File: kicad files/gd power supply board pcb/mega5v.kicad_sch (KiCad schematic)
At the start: 14 parts

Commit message: before erc
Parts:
- added H10, H11, H12, H9: MountingHole, MountingHole:MountingHole_2.2mm_M2, symbol Mechanical:MountingHole
- gave numbers to parts that had none: 14
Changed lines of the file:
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@@
   (symbol (lib_id "Device:R_Small") (at 171.45 105.41 180) (unit 1)
     (in_bom yes) (on_board yes)
-    (property "Reference" "R?" (id 0) (at 172.9486 104.2416 0)
+    (property "Reference" "R23" (id 0) (at 172.9486 104.2416 0)
       (effects (font (size 1.27 1.27)) (justify right))
     )
@@
     (pin "2")
   )
+  (symbol (lib_id "Mechanical:MountingHole") (at 200.66 53.34 0) (unit 1)
+    (in_bom yes) (on_board yes) (fields_autoplaced)
+    (property "Reference" "H9" (id 0) (at 203.2 52.0699 0)
+      (effects (font (size 1.27 1.27)) (justify left))
+    )
+    (property "Value" "MountingHole" (id 1) (at 203.2 54.6099 0)
+      (effects (font (size 1.27 1.27)) (justify left))
+    )
+    (property "Footprint" "MountingHole:MountingHole_2.2mm_M2" (id 2) (at 200.66 53.34 0)
+      (effects (font (size 1.27 1.27)) hide)
+    )
+    (property "Datasheet" "~" (id 3) (at 200.66 53.34 0)
+      (effects (font (size 1.27 1.27)) hide)
+    )
+  )
   (symbol (lib_id "My Library:TestPoint_Harwin") (at 171.45 93.98 0) (unit 1)
     (in_bom yes) (on_board yes)
-    (property "Reference" "TP?" (id 0) (at 170.18 88.9 0)
+    (property "Reference" "TP25" (id 0) (at 170.18 88.9 0)
       (effects (font (size 1.27 1.27)) (justify left))
     )
@@
   (symbol (lib_id "power:GND") (at 171.45 109.728 0) (unit 1)
     (in_bom yes) (on_board yes)
-    (property "Reference" "#PWR?" (id 0) (at 171.45 116.078 0)
+    (property "Reference" "#PWR05" (id 0) (at 171.45 116.078 0)
       (effects (font (size 1.27 1.27)) hide)
     )
@@
   (symbol (lib_id "My Library:TestPoint_Harwin") (at 125.73 99.06 180) (unit 1)
     (in_bom yes) (on_board yes)
-    (property "Reference" "TP?" (id 0) (at 124.46 105.41 0)
+    (property "Reference" "TP22" (id 0) (at 124.46 105.41 0)
       (effects (font (size 1.27 1.27)) (justify right))
     )
@@
   (symbol (lib_id "power:GND") (at 195.58 101.854 0) (unit 1)
     (in_bom yes) (on_board yes)
-    (property "Reference" "#PWR?" (id 0) (at 195.58 108.204 0)
+    (property "Reference" "#PWR07" (id 0) (at 195.58 108.204 0)
       (effects (font (size 1.27 1.27)) hide)
     )
@@
   (symbol (lib_id "Device:R_Small") (at 171.45 97.282 180) (unit 1)
     (in_bom yes) (on_board yes)
-    (property "Reference" "R?" (id 0) (at 172.9486 96.1136 0)
+    (property "Reference" "R22" (id 0) (at 172.9486 96.1136 0)
       (effects (font (size 1.27 1.27)) (justify right))
     )
@@
   (symbol (lib_id "Device:L_Small") (at 165.1 93.98 90) (unit 1)
     (in_bom yes) (on_board yes)
-    (property "Reference" "L?" (id 0) (at 165.1 89.281 90))
+    (property "Reference" "L3" (id 0) (at 165.1 89.281 90))
     (property "Value" "1.5u" (id 1) (at 165.1 91.5924 90))
     (property "Footprint" "Inductor_SMD:L_Bourns_SRP5030T" (id 2) (at 165.1 93.98 0)
@@
   (symbol (lib_id "power:GND") (at 100.33 102.87 0) (unit 1)
     (in_bom yes) (on_board yes)
-    (property "Reference" "#PWR?" (id 0) (at 100.33 109.22 0)
+    (property "Reference" "#PWR02" (id 0) (at 100.33 109.22 0)
       (effects (font (size 1.27 1.27)) hide)
     )
@@
   (symbol (lib_id "Device:C_Small") (at 154.94 85.344 0) (unit 1)
     (in_bom yes) (on_board yes)
-    (property "Reference" "C?" (id 0) (at 157.2768 84.1756 0)
+    (property "Reference" "C14" (id 0) (at 157.2768 84.1756 0)
       (effects (font (size 1.27 1.27)) (justify left))
     )
@@
   (symbol (lib_id "My Library:TestPoint_Harwin") (at 158.75 99.06 180) (unit 1)
     (in_bom yes) (on_board yes) (fields_autoplaced)
-    (property "Reference" "TP?" (id 0) (at 161.29 102.3619 0)
+    (property "Reference" "TP24" (id 0) (at 161.29 102.3619 0)
       (effects (font (size 1.27 1.27)) (justify right))
     )
@@
   (symbol (lib_id "Device:C_Small") (at 109.22 99.06 0) (unit 1)
     (in_bom yes) (on_board yes)
-    (property "Reference" "C?" (id 0) (at 111.5568 97.8916 0)
+    (property "Reference" "C13" (id 0) (at 111.5568 97.8916 0)
       (effects (font (size 1.27 1.27)) (justify left))
     )
@@
   (symbol (lib_id "Device:C_Small") (at 195.58 97.536 0) (unit 1)
     (in_bom yes) (on_board yes)
-    (property "Reference" "C?" (id 0) (at 197.9168 96.3676 0)
+    (property "Reference" "C16" (id 0) (at 197.9168 96.3676 0)
       (effects (font (size 1.27 1.27)) (justify left))
     )
@@
   (symbol (lib_id "My Library:TestPoint_Harwin") (at 109.22 93.98 0) (unit 1)
     (in_bom yes) (on_board yes)
-    (property "Reference" "TP?" (id 0) (at 107.95 88.9 0)
+    (property "Reference" "TP21" (id 0) (at 107.95 88.9 0)
       (effects (font (size 1.27 1.27)) (justify left))
     )
@@
   (symbol (lib_id "TO3-Switching-Supply-rescue:TPS563200-Regulator_Switching") (at 137.16 96.52 0) (unit 1)
     (in_bom yes) (on_board yes)
-    (property "Reference" "U?" (id 0) (at 137.16 87.1982 0))
+    (property "Reference" "U3" (id 0) (at 137.16 87.1982 0))
     (property "Value" "TPS563240DDCR" (id 1) (at 137.16 89.5096 0))
     (property "Footprint" "Package_TO_SOT_SMD:SOT-23-6" (id 2) (at 138.43 102.87 0)
@@
   (symbol (lib_id "Device:C_Small") (at 185.42 97.79 0) (unit 1)
     (in_bom yes) (on_board yes)
-    (property "Reference" "C?" (id 0) (at 187.7568 96.6216 0)
+    (property "Reference" "C15" (id 0) (at 187.7568 96.6216 0)
       (effects (font (size 1.27 1.27)) (justify left))
     )
@@
   (symbol (lib_id "power:GND") (at 109.22 102.87 0) (unit 1)
     (in_bom yes) (on_board yes)
-    (property "Reference" "#PWR?" (id 0) (at 109.22 109.22 0)
+    (property "Reference" "#PWR03" (id 0) (at 109.22 109.22 0)
       (effects (font (size 1.27 1.27)) hide)
     )
@@
   (symbol (lib_id "power:GND") (at 137.16 106.68 0) (unit 1)
     (in_bom yes) (on_board yes)
-    (property "Reference" "#PWR?" (id 0) (at 137.16 113.03 0)
+    (property "Reference" "#PWR04" (id 0) (at 137.16 113.03 0)
       (effects (font (size 1.27 1.27)) hide)
     )
@@
   (symbol (lib_id "power:GND") (at 185.42 102.108 0) (unit 1)
     (in_bom yes) (on_board yes)
-    (property "Reference" "#PWR?" (id 0) (at 185.42 108.458 0)
+    (property "Reference" "#PWR06" (id 0) (at 185.42 108.458 0)
       (effects (font (size 1.27 1.27)) hide)
     )
@@
     (pin "1")
   )
+  (symbol (lib_id "Mechanical:MountingHole") (at 209.55 53.34 0) (unit 1)
+    (in_bom yes) (on_board yes) (fields_autoplaced)
+    (property "Reference" "H11" (id 0) (at 212.09 52.0699 0)
+      (effects (font (size 1.27 1.27)) (justify left))
+    )
+    (property "Value" "MountingHole" (id 1) (at 212.09 54.6099 0)
+      (effects (font (size 1.27 1.27)) (justify left))
+    )
+    (property "Footprint" "MountingHole:MountingHole_2.2mm_M2" (id 2) (at 209.55 53.34 0)
+      (effects (font (size 1.27 1.27)) hide)
+    )
+    (property "Datasheet" "~" (id 3) (at 209.55 53.34 0)
+      (effects (font (size 1.27 1.27)) hide)
+    )
+  )
   (symbol (lib_id "My Library:TestPoint_Harwin") (at 158.75 93.98 0) (unit 1)
     (in_bom yes) (on_board yes)
-    (property "Reference" "TP?" (id 0) (at 157.48 88.9 0)
+    (property "Reference" "TP23" (id 0) (at 157.48 88.9 0)
       (effects (font (size 1.27 1.27)) (justify left))
     )
@@
     (pin "1")
   )
+  (symbol (lib_id "Mechanical:MountingHole") (at 209.55 59.69 0) (unit 1)
+    (in_bom yes) (on_board yes) (fields_autoplaced)
+    (property "Reference" "H12" (id 0) (at 212.09 58.4199 0)
+      (effects (font (size 1.27 1.27)) (justify left))
+    )
+    (property "Value" "MountingHole" (id 1) (at 212.09 60.9599 0)
+      (effects (font (size 1.27 1.27)) (justify left))
+    )
+    (property "Footprint" "MountingHole:MountingHole_2.2mm_M2" (id 2) (at 209.55 59.69 0)
+      (effects (font (size 1.27 1.27)) hide)
+    )
+    (property "Datasheet" "~" (id 3) (at 209.55 59.69 0)
+      (effects (font (size 1.27 1.27)) hide)
+    )
+  )
   (symbol (lib_id "Device:C_Small") (at 100.33 97.79 0) (unit 1)
     (in_bom yes) (on_board yes)
-    (property "Reference" "C?" (id 0) (at 102.6668 96.6216 0)
+    (property "Reference" "C12" (id 0) (at 102.6668 96.6216 0)
       (effects (font (size 1.27 1.27)) (justify left))
     )
@@
     (pin "2")
   )
+  (symbol (lib_id "Mechanical:MountingHole") (at 200.66 59.69 0) (unit 1)
+    (in_bom yes) (on_board yes) (fields_autoplaced)
+    (property "Reference" "H10" (id 0) (at 203.2 58.4199 0)
+      (effects (font (size 1.27 1.27)) (justify left))
+    )
+    (property "Value" "MountingHole" (id 1) (at 203.2 60.9599 0)
+      (effects (font (size 1.27 1.27)) (justify left))
+    )
+    (property "Footprint" "MountingHole:MountingHole_2.2mm_M2" (id 2) (at 200.66 59.69 0)
+      (effects (font (size 1.27 1.27)) hide)
+    )
+    (property "Datasheet" "~" (id 3) (at 200.66 59.69 0)
+      (effects (font (size 1.27 1.27)) hide)
+    )
+  )
 )

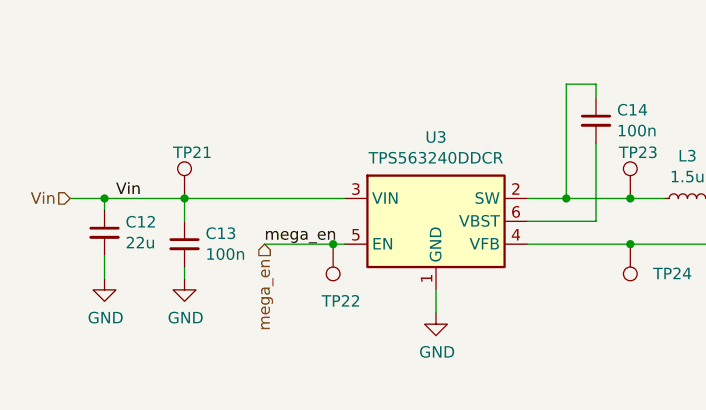
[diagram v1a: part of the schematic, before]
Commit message: initial floor planning done
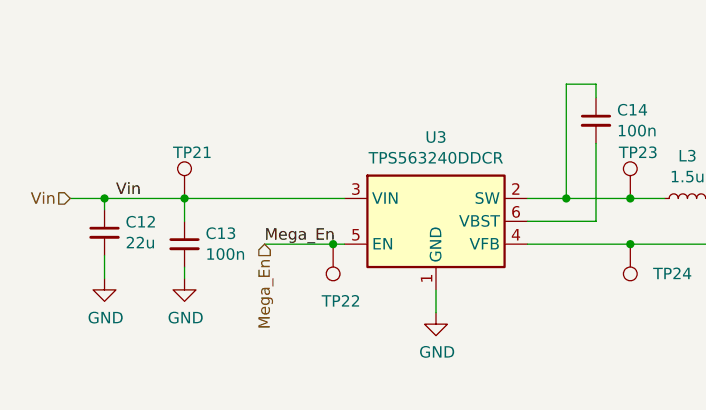
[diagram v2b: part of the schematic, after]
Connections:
- net mega_en renamed Mega_En
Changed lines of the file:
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@@
     (effects (font (size 1.27 1.27)) (justify left bottom))
   )
-  (label "mega_en" (at 118.11 99.06 0)
+  (label "Mega_En" (at 118.11 99.06 0)
     (effects (font (size 1.27 1.27)) (justify left bottom))
   )
@@
     (effects (font (size 1.27 1.27)) (justify right))
   )
-  (hierarchical_label "mega_en" (shape input) (at 118.11 99.06 270)
+  (hierarchical_label "Mega_En" (shape input) (at 118.11 99.06 270)
     (effects (font (size 1.27 1.27)) (justify right))
   )

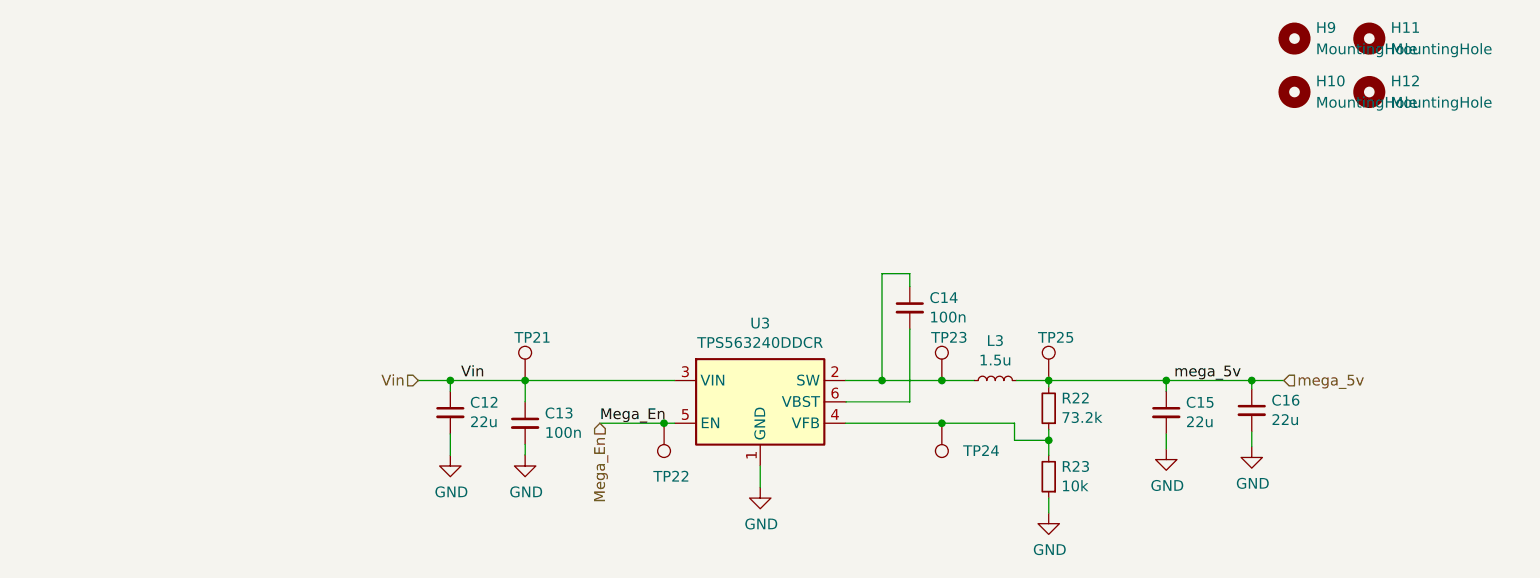
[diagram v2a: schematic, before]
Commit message: minor fixes and compacting the floorplan. stacked 5V supplies for maximum minimage.
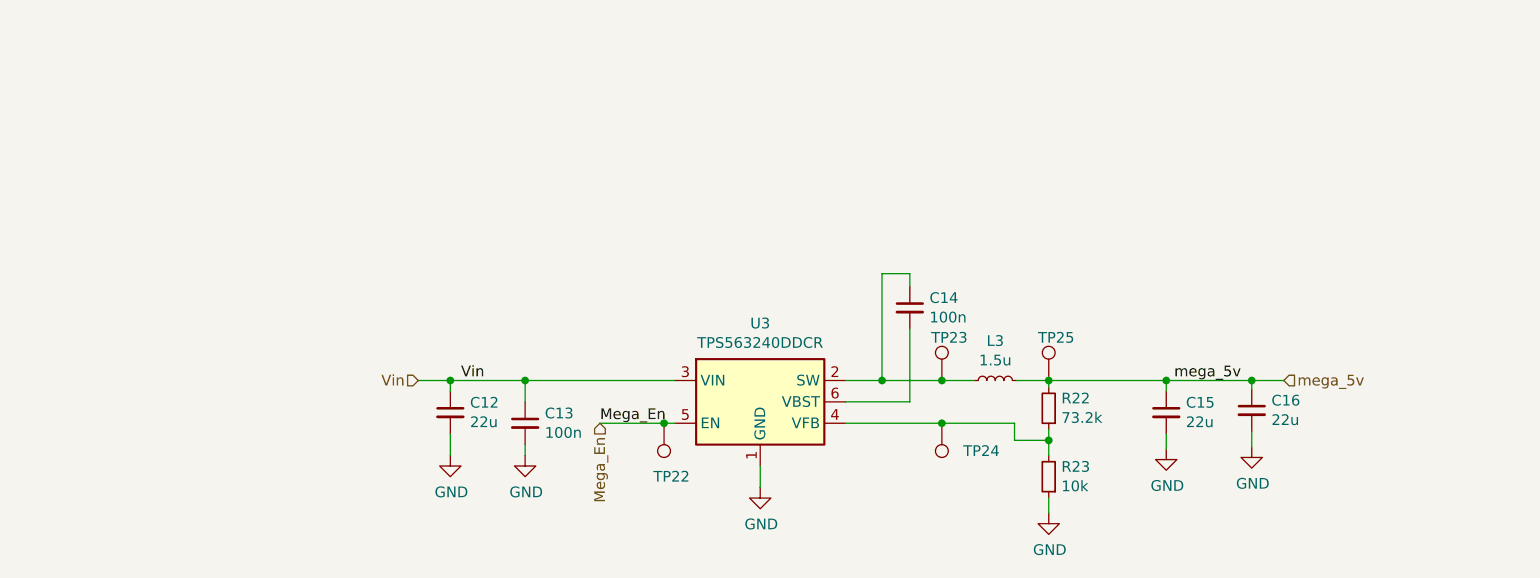
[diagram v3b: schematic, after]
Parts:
- removed H10, H11, H12, H9: MountingHole, MountingHole:MountingHole_2.2mm_M2, symbol Mechanical:MountingHole
- removed TP21: TestPoint_Harwin, My Libraries:Harwin-S1751-46-Test-Point, symbol My Library:TestPoint_Harwin
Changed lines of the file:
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@@
     (pin "2")
-  )
-  (symbol (lib_id "Mechanical:MountingHole") (at 200.66 53.34 0) (unit 1)
-    (in_bom yes) (on_board yes) (fields_autoplaced)
-    (property "Reference" "H9" (id 0) (at 203.2 52.0699 0)
-      (effects (font (size 1.27 1.27)) (justify left))
-    )
-    (property "Value" "MountingHole" (id 1) (at 203.2 54.6099 0)
-      (effects (font (size 1.27 1.27)) (justify left))
-    )
-    (property "Footprint" "MountingHole:MountingHole_2.2mm_M2" (id 2) (at 200.66 53.34 0)
-      (effects (font (size 1.27 1.27)) hide)
-    )
-    (property "Datasheet" "~" (id 3) (at 200.66 53.34 0)
-      (effects (font (size 1.27 1.27)) hide)
-    )
   )
   (symbol (lib_id "My Library:TestPoint_Harwin") (at 171.45 93.98 0) (unit 1)
@@
     (pin "1")
     (pin "2")
-  )
-  (symbol (lib_id "My Library:TestPoint_Harwin") (at 109.22 93.98 0) (unit 1)
-    (in_bom yes) (on_board yes)
-    (property "Reference" "TP21" (id 0) (at 107.95 88.9 0)
-      (effects (font (size 1.27 1.27)) (justify left))
-    )
-    (property "Value" "TestPoint_Harwin" (id 1) (at 109.22 88.9 0)
-      (effects (font (size 1.27 1.27)) hide)
-    )
-    (property "Footprint" "My Libraries:Harwin-S1751-46-Test-Point" (id 2) (at 114.3 93.98 0)
-      (effects (font (size 1.27 1.27)) hide)
-    )
-    (property "Datasheet" "~" (id 3) (at 114.3 93.98 0)
-      (effects (font (size 1.27 1.27)) hide)
-    )
-    (pin "1")
   )
   (symbol (lib_id "TO3-Switching-Supply-rescue:TPS563200-Regulator_Switching") (at 137.16 96.52 0) (unit 1)
@@
     (pin "1")
   )
-  (symbol (lib_id "Mechanical:MountingHole") (at 209.55 53.34 0) (unit 1)
-    (in_bom yes) (on_board yes) (fields_autoplaced)
-    (property "Reference" "H11" (id 0) (at 212.09 52.0699 0)
-      (effects (font (size 1.27 1.27)) (justify left))
-    )
-    (property "Value" "MountingHole" (id 1) (at 212.09 54.6099 0)
-      (effects (font (size 1.27 1.27)) (justify left))
-    )
-    (property "Footprint" "MountingHole:MountingHole_2.2mm_M2" (id 2) (at 209.55 53.34 0)
-      (effects (font (size 1.27 1.27)) hide)
-    )
-    (property "Datasheet" "~" (id 3) (at 209.55 53.34 0)
-      (effects (font (size 1.27 1.27)) hide)
-    )
-  )
   (symbol (lib_id "My Library:TestPoint_Harwin") (at 158.75 93.98 0) (unit 1)
     (in_bom yes) (on_board yes)
@@
     (pin "1")
   )
-  (symbol (lib_id "Mechanical:MountingHole") (at 209.55 59.69 0) (unit 1)
-    (in_bom yes) (on_board yes) (fields_autoplaced)
-    (property "Reference" "H12" (id 0) (at 212.09 58.4199 0)
-      (effects (font (size 1.27 1.27)) (justify left))
-    )
-    (property "Value" "MountingHole" (id 1) (at 212.09 60.9599 0)
-      (effects (font (size 1.27 1.27)) (justify left))
-    )
-    (property "Footprint" "MountingHole:MountingHole_2.2mm_M2" (id 2) (at 209.55 59.69 0)
-      (effects (font (size 1.27 1.27)) hide)
-    )
-    (property "Datasheet" "~" (id 3) (at 209.55 59.69 0)
-      (effects (font (size 1.27 1.27)) hide)
-    )
-  )
   (symbol (lib_id "Device:C_Small") (at 100.33 97.79 0) (unit 1)
     (in_bom yes) (on_board yes)
@@
     (pin "2")
   )
-  (symbol (lib_id "Mechanical:MountingHole") (at 200.66 59.69 0) (unit 1)
-    (in_bom yes) (on_board yes) (fields_autoplaced)
-    (property "Reference" "H10" (id 0) (at 203.2 58.4199 0)
-      (effects (font (size 1.27 1.27)) (justify left))
-    )
-    (property "Value" "MountingHole" (id 1) (at 203.2 60.9599 0)
-      (effects (font (size 1.27 1.27)) (justify left))
-    )
-    (property "Footprint" "MountingHole:MountingHole_2.2mm_M2" (id 2) (at 200.66 59.69 0)
-      (effects (font (size 1.27 1.27)) hide)
-    )
-    (property "Datasheet" "~" (id 3) (at 200.66 59.69 0)
-      (effects (font (size 1.27 1.27)) hide)
-    )
-  )
 )

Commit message: pre-routing try 1
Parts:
- added JP4: mega_5v_jmp, Jumper:SolderJumper-2_P1.3mm_Open_TrianglePad1.0x1.5mm, symbol Jumper:Jumper_2_Open
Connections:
- net Vin: now also JP4.1 (A); no longer C12.1, C13.1, U3.3 (VIN)
- new net: C12.1, C13.1, JP4.2 (B), U3.3 (VIN)
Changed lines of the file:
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@@
+    (stroke (width 0) (type default) (color 0 0 0 0))
+  )
+  (wire (pts (xy 81.28 93.98) (xy 83.82 93.98))
     (stroke (width 0) (type default) (color 0 0 0 0))
   )
@@
     (stroke (width 0) (type default) (color 0 0 0 0))
   )
-  (wire (pts (xy 96.52 93.98) (xy 100.33 93.98))
+  (wire (pts (xy 93.98 93.98) (xy 100.33 93.98))
     (stroke (width 0) (type default) (color 0 0 0 0))
   )
@@
     (effects (font (size 1.27 1.27)) (justify right bottom))
   )
-  (label "Vin" (at 101.6 93.98 0)
-    (effects (font (size 1.27 1.27)) (justify left bottom))
-  )
   (label "Mega_En" (at 118.11 99.06 0)
     (effects (font (size 1.27 1.27)) (justify left bottom))
   )
-  (hierarchical_label "Vin" (shape input) (at 96.52 93.98 180)
-    (effects (font (size 1.27 1.27)) (justify right))
-  )
   (hierarchical_label "Mega_En" (shape input) (at 118.11 99.06 270)
     (effects (font (size 1.27 1.27)) (justify right))
@@
   (hierarchical_label "mega_5v" (shape input) (at 199.39 93.98 0)
     (effects (font (size 1.27 1.27)) (justify left))
+  )
+  (hierarchical_label "Vin" (shape input) (at 81.28 93.98 180)
+    (effects (font (size 1.27 1.27)) (justify right))
   )
   (symbol (lib_id "Device:R_Small") (at 171.45 105.41 180) (unit 1)
@@
     (pin "1")
   )
+  (symbol (lib_id "Jumper:Jumper_2_Open") (at 88.9 93.98 0) (unit 1)
+    (in_bom yes) (on_board yes) (fields_autoplaced)
+    (property "Reference" "JP4" (id 0) (at 88.9 87.63 0))
+    (property "Value" "mega_5v_jmp" (id 1) (at 88.9 90.17 0))
+    (property "Footprint" "Jumper:SolderJumper-2_P1.3mm_Open_TrianglePad1.0x1.5mm" (id 2) (at 88.9 93.98 0)
+      (effects (font (size 1.27 1.27)) hide)
+    )
+    (property "Datasheet" "~" (id 3) (at 88.9 93.98 0)
+      (effects (font (size 1.27 1.27)) hide)
+    )
+    (pin "1")
+    (pin "2")
+  )
   (symbol (lib_id "My Library:TestPoint_Harwin") (at 158.75 93.98 0) (unit 1)
